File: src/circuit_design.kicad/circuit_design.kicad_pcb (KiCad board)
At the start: 2 copper layers, 220.3 x 182.9 mm, 184 parts, among them J1 CONN_BAT, Q1 BT136-600, Q2 BT136-600, Q3 BT136-600, Q4 BT136-600, U1 К176ИЕ12, U10 К155ЛА4, U11 К155ЛИ1, U12 К155ЛА1, U13 К155ИЕ5, U14 К155ЛЛ1, U15 К155ЛН1, U16 К155ЛИ1, U17 К155ТВ15, U18 К155ИЕ5, U19 К155ЛП5, U2 К155ЛП10, U20 К155ИВ1, U21 К155ИД7, U22 К155ИД4, U23 К155ЛН1, U24 К155ЛП10, U25 MOC3062M, U26 MOC3062M, U27 MOC3062M, U28 MOC3062M, U29 LM7806_TO220, U3 К155ЛЕ3, U30 SC6038, U31 К155ЛЕ1, U32 К155ЛН1, U33 К155ЛИ1, U34 К155ЛА4, U35 К155ТВ15, U36 К155ТЛ2, U37 4020, U38 LM7806_TO220, U39 К155ЛН1, U4 К155ЛН1, U5 К155ЛИ1, U6 К155ЛЛ1, U7 4020, U8 ICL7660, U9 К155ИЕ5, Y1 32768

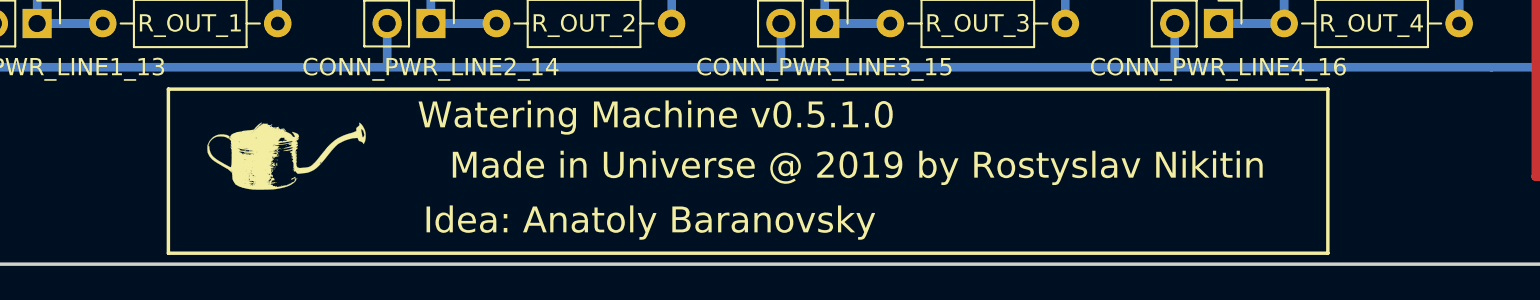
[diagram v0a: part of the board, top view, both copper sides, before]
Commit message: The README.md file was updated:   - The PCB 3D layout was added
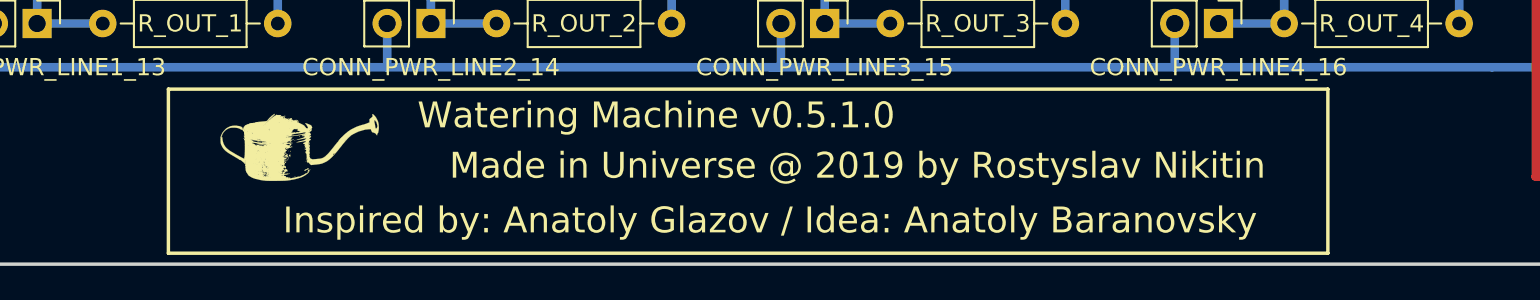
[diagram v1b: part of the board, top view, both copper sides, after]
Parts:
- moved G*** 0.92 mm to (116.8, 184.8)
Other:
- board text added: "Inspired by: Anatoly Glazov / Idea: Anatoly Baranovsky"
- board text removed: "Idea: Anatoly Baranovsky"
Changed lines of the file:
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@@
   )
   (module logo:logo locked (layer F.Cu)
-    (at 116.078 185.293)
+    (at 116.84 184.785)
     (fp_text reference G*** (at 0 0) (layer F.SilkS) hide
       (effects (font (size 1.524 1.524) (thickness 0.3)))
@@
     )
   )
+  (gr_text "Inspired by: Anatoly Glazov / Idea: Anatoly Baranovsky" (at 144.145 189.23) (layer F.SilkS)
+    (effects (font (size 1.5 1.5) (thickness 0.3)))
+  )
   (dimension 182.88 (width 0.3) (layer F.SilkS)
     (gr_text "182.880 mm" (at 277.69 100.33 270) (layer F.SilkS)
@@
   )
   (target plus (at 256.276491 141.543188) (size 5) (width 0.15) (layer Edge.Cuts))
-  (gr_text "Idea: Anatoly Baranovsky" (at 137.16 189.23) (layer F.SilkS)
-    (effects (font (size 1.5 1.5) (thickness 0.3)))
-  )
   (gr_line (start 263.525 8.89) (end 263.525 191.77) (layer Edge.Cuts) (width 0.2))
   (gr_line (start 43.18 191.77) (end 43.18 8.89) (layer Edge.Cuts) (width 0.2))

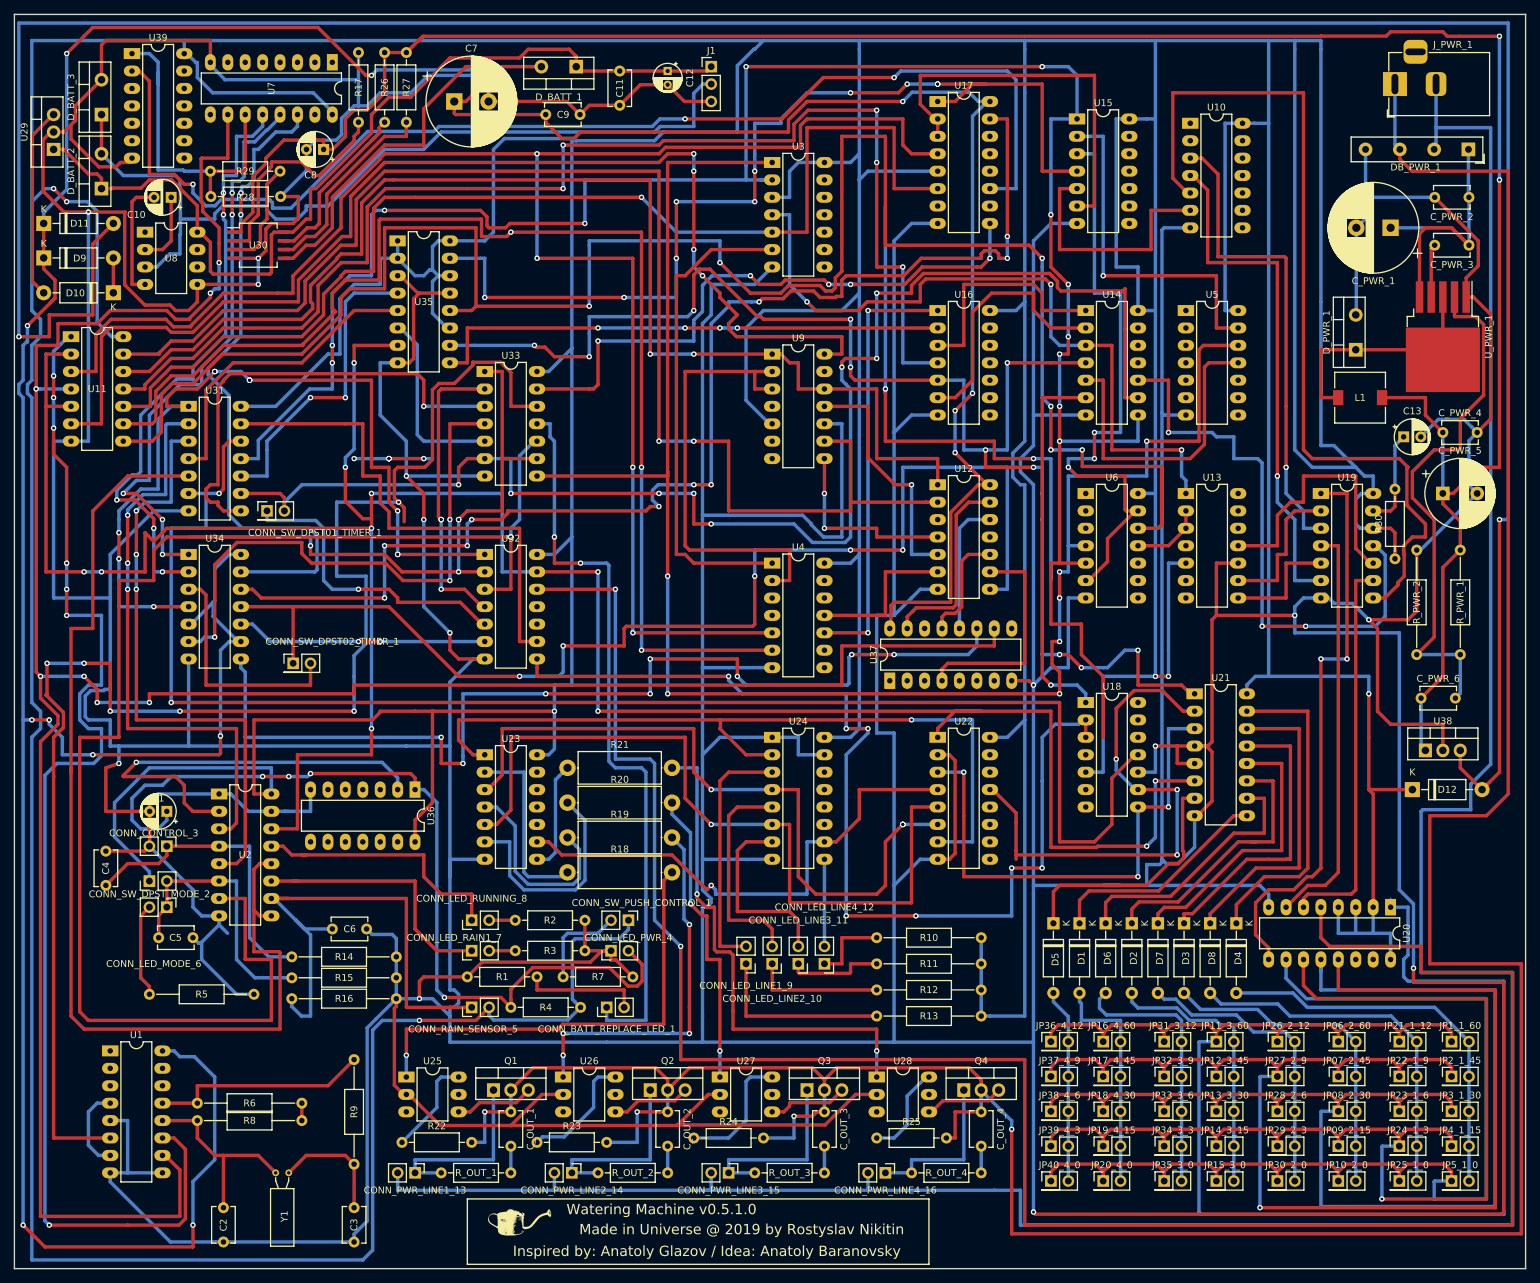
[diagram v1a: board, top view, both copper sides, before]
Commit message: 01. The "Init" signal label was added 02. The "Init" signal was used to reset the running state and the battery timer triggers 03. Shmidt triggers was added to the Control(Ext.2) and Mode(Ext.) inputs
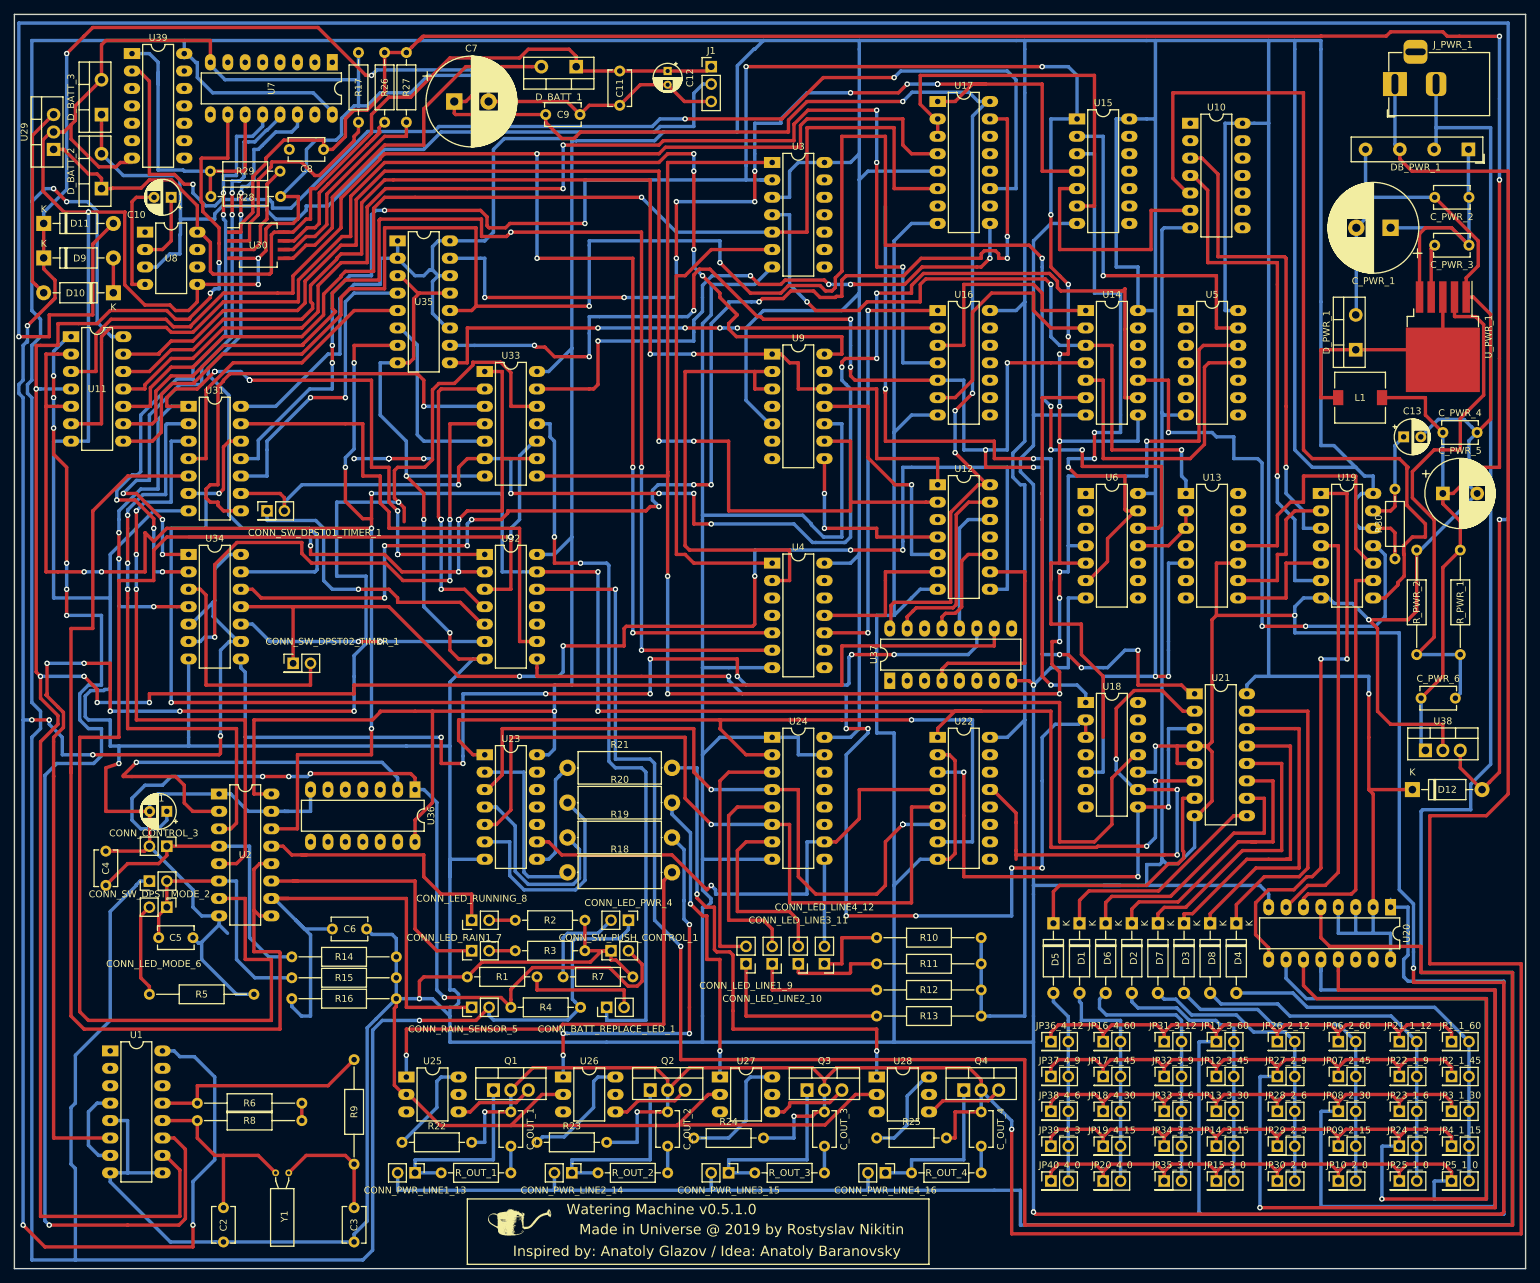
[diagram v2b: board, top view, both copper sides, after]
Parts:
- C8: footprint Capacitor_THT:CP_Radial_D5.0mm_P2.50mm -> Capacitor_THT:C_Disc_D5.1mm_W3.2mm_P5.00mm
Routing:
- net +5V: track 1829.0 -> 1847.7 mm

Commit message: 01. The connectors was placed to the external signals near to chips (to avoid long lines) 02. The LM7806(U38) was put to the board to dissipate heat
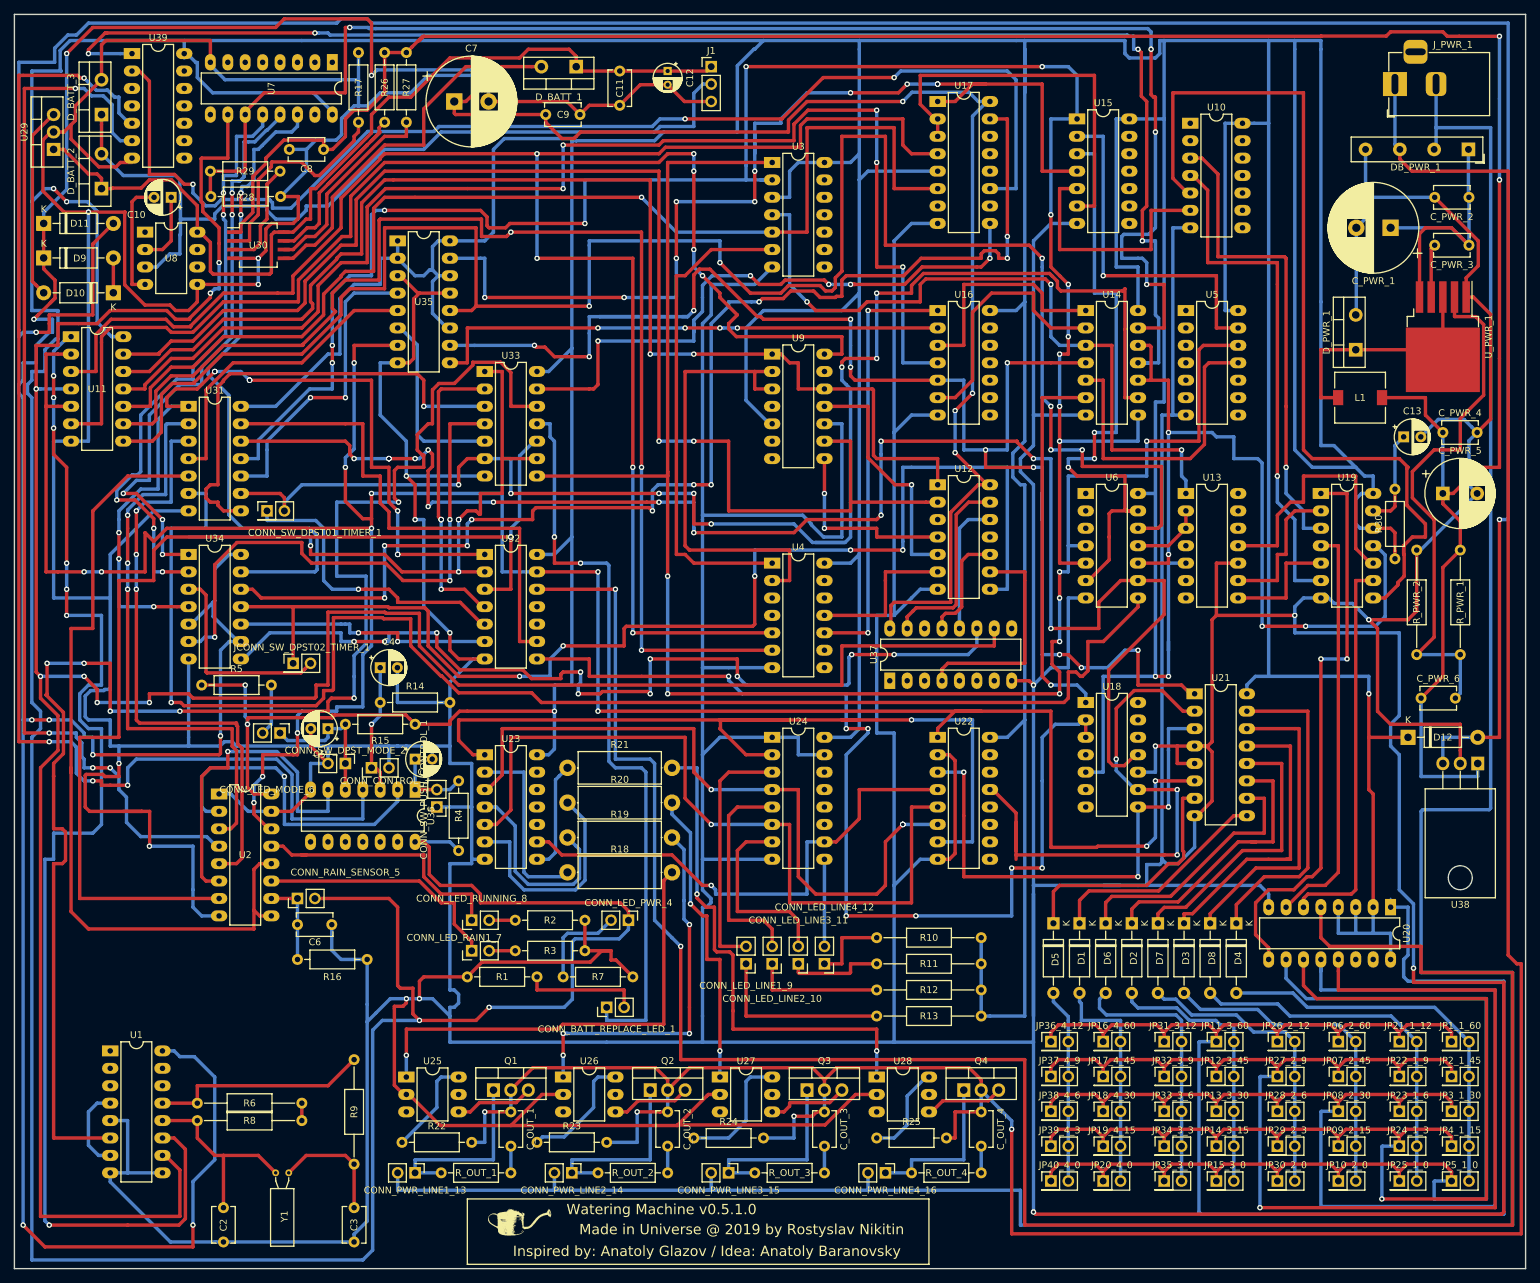
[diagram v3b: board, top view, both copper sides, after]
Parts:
- removed CONN_SW_DPST02_TIMER_1: Conn_01x02_Male, Connector_PinHeader_2.54mm:PinHeader_2x01_P2.54mm_Vertical
- added JCONN_SW_DPST02_TIMER_1: Conn_01x02_Male, Connector_PinHeader_2.54mm:PinHeader_2x01_P2.54mm_Vertical, F.Cu at (83.8, 103.5)
- C4, C5: value 474 -> 100uF; footprint Capacitor_THT:C_Disc_D5.1mm_W3.2mm_P5.00mm -> Capacitor_THT:CP_Radial_D5.0mm_P2.50mm
- C_OUT_1: value 105 -> 103
- C_OUT_2, C_OUT_3, C_OUT_4: value 106 -> 103
- D1, D2, D3, D4, D5, D6, D7, D8: value 1N4007 -> 1N5817
- R14, R15, R16, R5: footprint Resistor_THT:R_Axial_DIN0207_L6.3mm_D2.5mm_P15.24mm_Horizontal -> Resistor_THT:R_Axial_DIN0207_L6.3mm_D2.5mm_P10.16mm_Horizontal
- R30: value 1K -> 10K
- U38: footprint Package_TO_SOT_THT:TO-220-3_Vertical -> Package_TO_SOT_THT:TO-220-3_Horizontal_TabDown
- moved C4 51.1 mm to (96.5, 104.1), turned to 0 degrees
- moved R5 45.7 mm to (70.5, 106.7)
- moved R15 41.1 mm to (101.6, 112.4), turned to 180 degrees
- moved R14 39.3 mm to (96.5, 109.2)
- moved C5 39.2 mm to (88.9, 113.0), turned to 180 degrees
- moved C1 37.0 mm to (101.6, 117.5), turned to 0 degrees
- moved CONN_SW_DPST_MODE_2 33.3 mm to (91.4, 118.1), turned to 270 degrees
- moved CONN_SW_PUSH_CONTROL_1 32.9 mm to (104.8, 124.5), turned to 180 degrees
- moved CONN_CONTROL_3 32.0 mm to (95.2, 118.7), turned to 90 degrees
- moved CONN_LED_MODE_6 30.3 mm to (81.9, 113.7)
- moved CONN_RAIN_SENSOR_5 30.0 mm to (84.5, 137.8)
- moved R4 29.0 mm to (108.0, 130.8), turned to 90 degrees
- moved U38 7.85 mm to (256.5, 118.1), turned to 180 degrees
- moved D12 7.65 mm to (246.4, 114.3)
- moved R16 5.78 mm to (84.5, 146.7)
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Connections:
- C4 pad 1: /Control(Ext.2) -> Net-(C4-Pad1)
- C5 pad 1: /Mode(Ext.) -> Net-(C5-Pad1)
- CONN_CONTROL_3 pad 1: /Control(Ext.2) -> Net-(C4-Pad1)
- CONN_LED_MODE_6 pad 1: /Mode(Ext.) -> Net-(C5-Pad1)
- CONN_SW_DPST_MODE_2 pad 1: +5V -> Net-(C5-Pad1)
- CONN_SW_DPST_MODE_2 pad 2: /Mode(Ext.) -> GND
- R14 pad 1: /Control(Ext.2) -> Net-(C4-Pad1)
- R15 pad 1: /Mode(Ext.) -> +5V
- R15 pad 2: GND -> Net-(C5-Pad1)
- R5 pad 1: Net-(CONN_LED_MODE_6-Pad2) -> +5V
- R5 pad 2: GND -> Net-(CONN_LED_MODE_6-Pad2)
- U14 pad 10: Net-(U14-Pad10) -> Init
- U14 pad 11: (no net) -> Net-(U14-Pad11)
- U14 pad 12: (no net) -> Init
- U14 pad 13: (no net) -> Net-(R28-Pad2)
- U18 pad 11: /Completed(In) -> Net-(U18-Pad11)
- U19 pad 11: Net-(U14-Pad10) -> Init
- U31 pad 12: /Completed(In) -> Net-(U18-Pad11)
- U36 pad 3: (no net) -> Net-(C4-Pad1)
- U36 pad 4: (no net) -> Net-(U36-Pad4)
- U36 pad 5: (no net) -> Net-(C5-Pad1)
- U36 pad 6: (no net) -> /Mode(Ext.)
- U39 pad 1: Net-(R28-Pad2) -> Net-(U14-Pad11)
- U39 pad 5: (no net) -> Net-(U36-Pad4)
- U39 pad 6: (no net) -> /Control(Ext.2)
- U6 pad 10: (no net) -> Init
- U6 pad 8: (no net) -> /Completed(In)
- U6 pad 9: (no net) -> Net-(U18-Pad11)
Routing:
- net Net-(U18-Pad11): track 0.00 -> 229.5 mm, vias 0 -> 14
- net Net-(U14-Pad11): track 0.00 -> 216.4 mm, vias 0 -> 4
- net Net-(U36-Pad4): track 0.00 -> 188.1 mm, vias 0 -> 4
- net Net-(R28-Pad2): track 46.5 -> 217.9 mm, vias 0 -> 4
- net Net-(C1-Pad1): track 128.4 -> 11.3 mm, vias 4 -> 0
- net Init: track 0.00 -> 113.4 mm, vias 0 -> 4
- net /Control(Ext.2): track 44.8 -> 156.0 mm, vias 0 -> 4
- net Net-(U14-Pad10): track 83.0 -> 0.00 mm, vias 3 -> 0
- net Net-(U17-Pad1): track 80.0 -> 0.00 mm, vias 2 -> 0
- net /Rain_Sensor(Ext.): track 77.7 -> 13.1 mm
- net /Mode(In): track 212.0 -> 162.0 mm
- net GND: track 2169.2 -> 2211.6 mm, vias 14 -> 16
- net /Rain(In): track 157.6 -> 120.5 mm
- net /Reset(Out): track 311.6 -> 279.1 mm
- net +5V: track 1847.7 -> 1871.6 mm, vias 7 -> 10
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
